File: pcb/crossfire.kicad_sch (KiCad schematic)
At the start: 4 parts

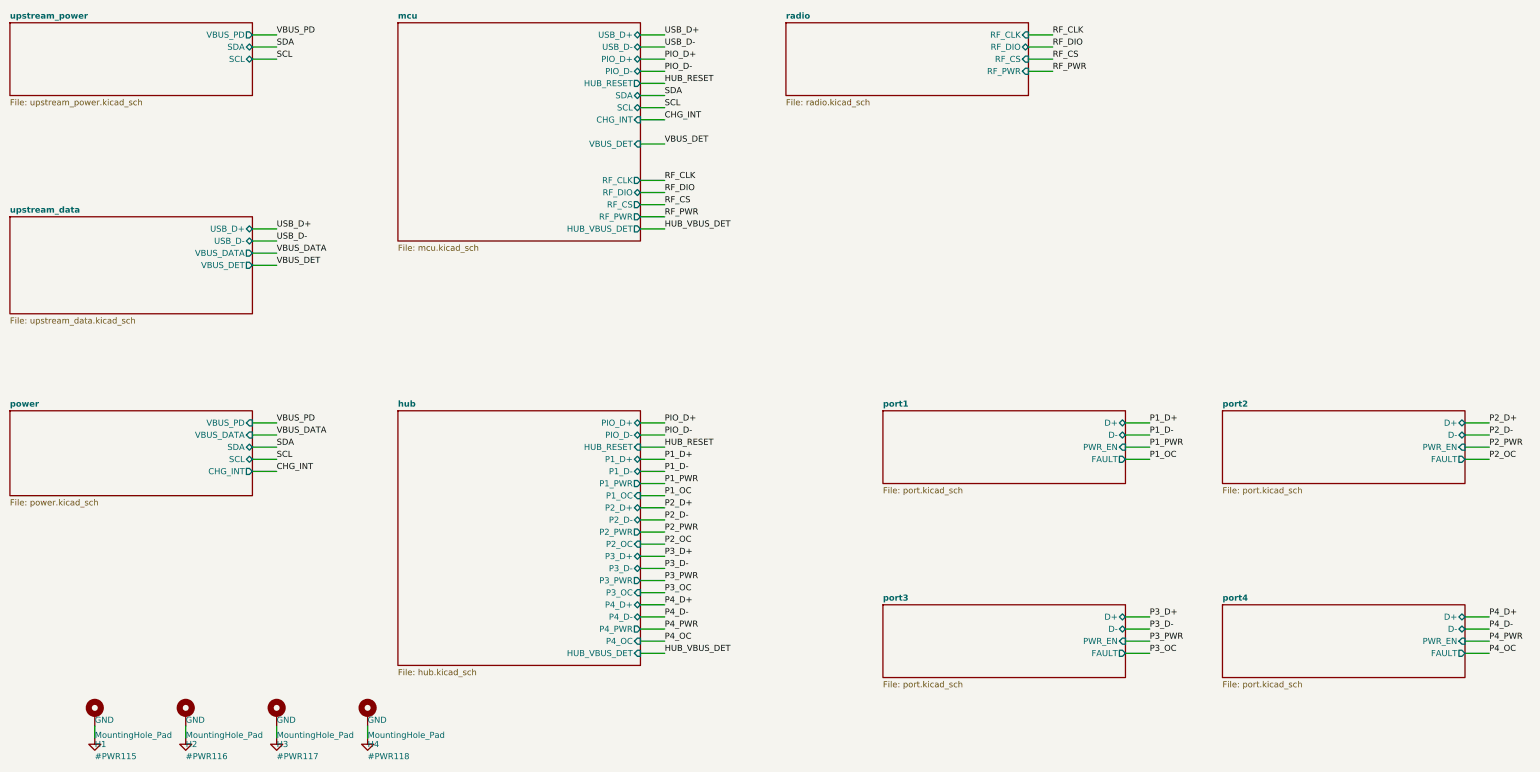
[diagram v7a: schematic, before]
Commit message: reduce the board to a single USB-C input
The PD sink and its connector, the charger and the cell, the input and ship
switches, the 5 V boost, the 3.3 V buck-boost and the radio come off. The
one remaining USB-C receptacle carries data to the hardware controller and
its VBUS is the 5 V rail: straight to the four port switches, and to a
fixed 3.3 V buck (AP63203) for everything else.

The two CC pins are read by ADC inputs through 10k into 100n, in series so
the 5.1k termination is not loaded, so firmware can tell a 3 A source from
a 1.5 A one from a default port and power the ports to fit.

Schematic: radio and upstream_power sheets removed, power sheet redrawn,
seven MCU pins freed and two taken. Board: 61 footprints and 514 tracks and
vias removed, survivors re-netted from the netlist, new parts loaded but
not placed. The layout is to be redone and the design document says so; it
is rewritten for this design, with what the single input gives up stated.

Co-Authored-By: Claude Fable 5.1 <noreply@anthropic.com>
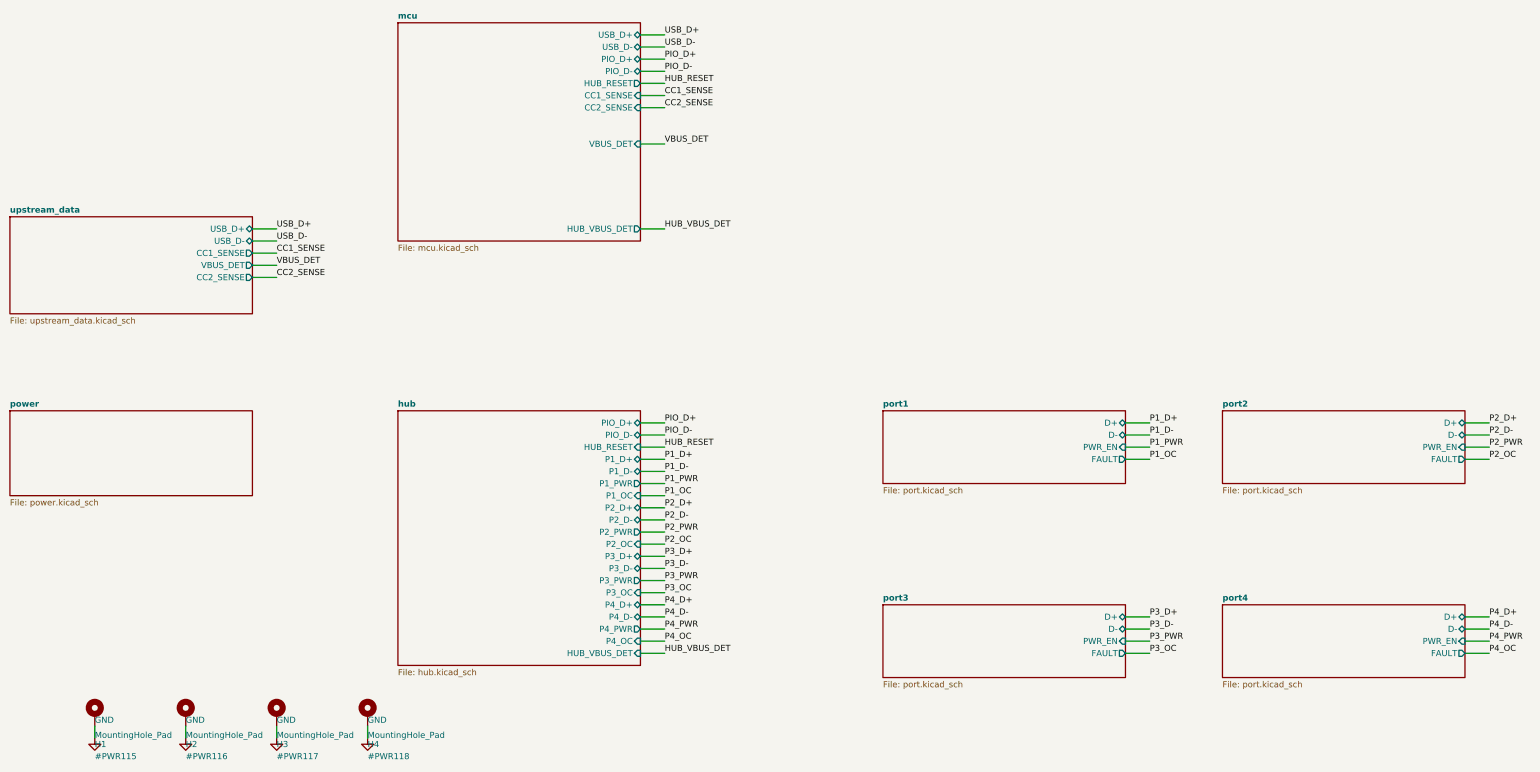
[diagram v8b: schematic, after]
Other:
- removed sheet radio
- removed sheet upstream_power
- sheet mcu ports: added CC1_SENSE, CC2_SENSE; removed CHG_INT, RF_CLK, RF_CS, RF_DIO, RF_PWR, SCL, SDA
- sheet power ports: added none; removed CHG_INT, SCL, SDA, VBUS_DATA, VBUS_PD
- sheet upstream_data ports: added CC1_SENSE, CC2_SENSE; removed VBUS_DATA
